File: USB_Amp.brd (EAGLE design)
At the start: 94 x 64 mm, 173 parts, among them CON1 USB-C-2OZ, CON2 PROG, CON3 PWR IN, CON5 SWD, CON6 USB-C-2OZ, IC1 3.3V, IC2 PIC32MZEF, IC3 TAS6422, IC4 3.3V, IC5 3.3V, IC6 TL431, IC7 STM32G030F, IC8 7805, IC9 CH221, Q1 NPN, Q2 NPN, Q3 PNP, Q4 PNP, X1 24.576MHz, X3 12MHz

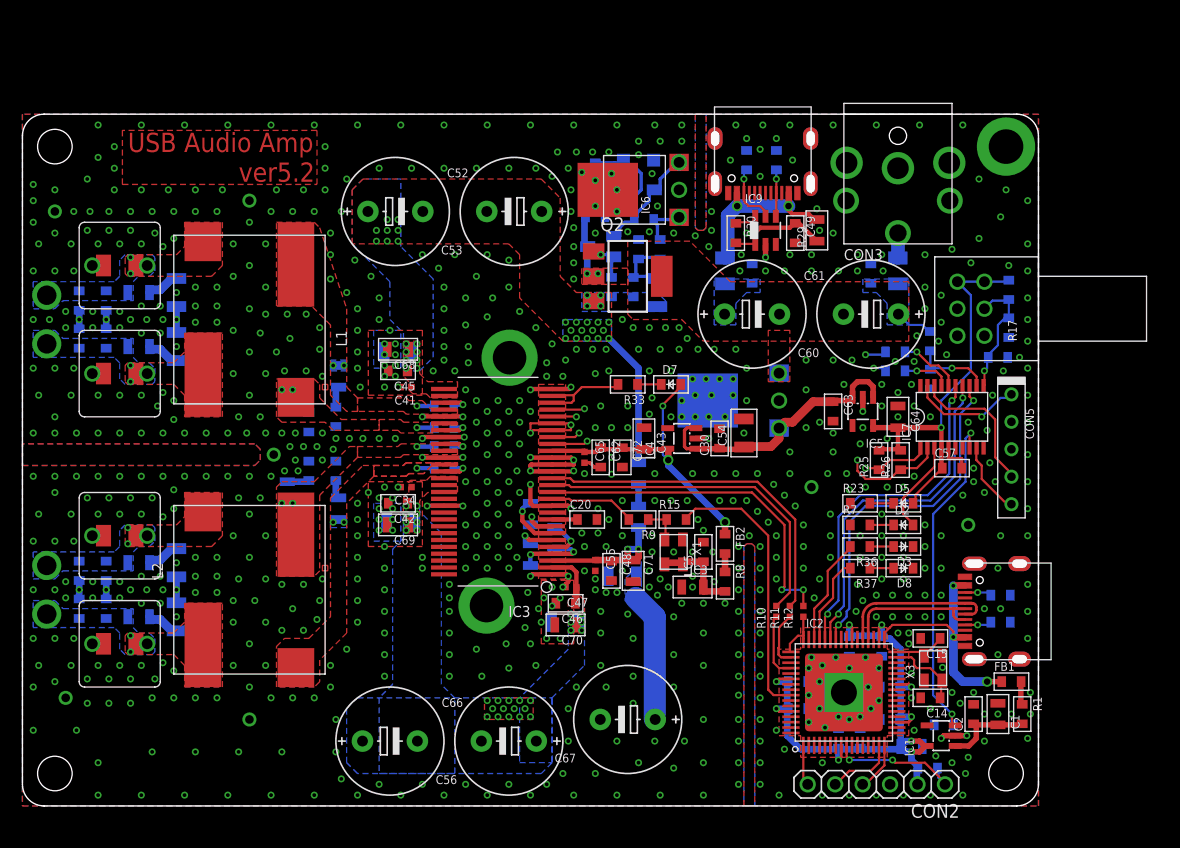
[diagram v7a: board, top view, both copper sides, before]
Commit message: TAS6424対応
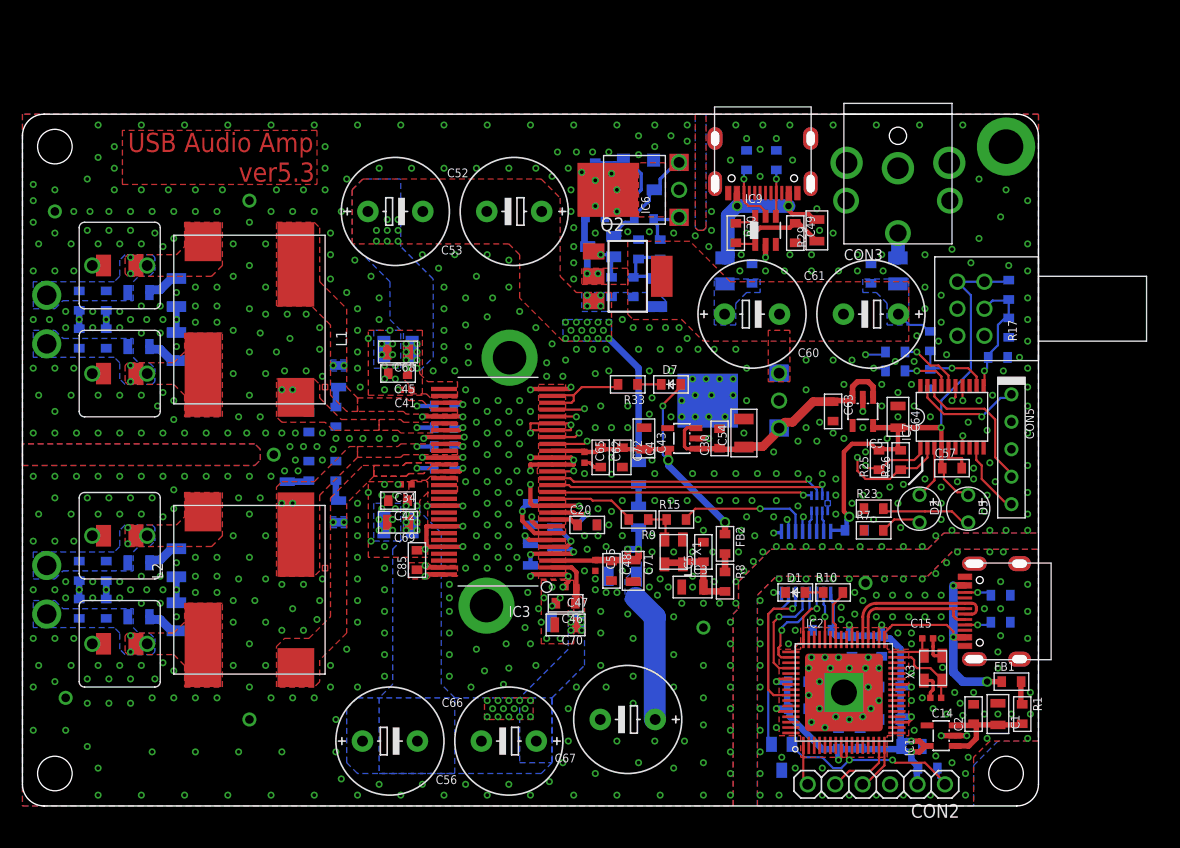
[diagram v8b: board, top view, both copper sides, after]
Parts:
- removed D3: LED1, my_rcl:D1608
- removed D8: LED2, my_rcl:D1608
- removed R11: DATA, my_rcl:1005
- removed R12: SCK, my_rcl:1005
- removed R36, R37: 3.3k, my_rcl:1608
- added C82, C83, C85: 0.1u, my_rcl:1608C
- added C84: 2.2u, my_rcl:1608C
- added D1: PLY, my_rcl:D1608
- added IC10: ISO7762, my_ic:TSSOP16
- added Q5: PNP, my_ic:SC59
- C14, C15: device my_rcl:1608C -> my_rcl:1005
- C74, C75: device my_rcl:3216 -> my_rcl:3225
- D2, D5: device my_rcl:D1608 -> my_rcl:LED2.5
- R10: value LRCLK -> 3.3k; device my_rcl:1005 -> my_rcl:1608
- R23, R7: value 3.3k -> 1.5k
- R6: value 10k -> 100; device my_rcl:1608 -> my_rcl:EXB28V
- moved TP10 26.3 mm to (63.0, 16.5)
- moved R6 23.5 mm to (73.8, 28.0)
- moved TP9 10.2 mm to (78.0, 20.6), turned to 0 degrees
- moved D5 6.02 mm to (87.5, 27.5), turned to 270 degrees
- moved R10 5.53 mm to (75.0, 19.8), turned to 0 degrees
- moved D2 2.12 mm to (83.0, 27.5), turned to 270 degrees
- moved R23 1.35 mm to (78.8, 27.5)
- moved R7 1.35 mm to (78.8, 25.5)
- moved C14 0.50 mm to (84.5, 10.0)
- moved C20 0.50 mm to (52.2, 26.0)
- moved C74 0.35 mm to (34.8, 26.0)
- moved C15 0.25 mm to (83.8, 15.5), turned to 0 degrees
- moved C34 0.25 mm to (35.5, 29.8)
- moved C41 0.25 mm to (35.5, 38.5)
- moved C42 0.25 mm to (34.8, 28.2)
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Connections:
- removed net EN_DDC: IC1.3, IC7.8, R6.1
- removed net LED2: IC2.45, R37.2
- removed net N$40: IC2.48, IC2.49, R12.1
- removed net N$41: IC2.50, R11.1
- removed net N$43: IC2.52, R10.1
- removed net N$44: D8.A, R37.1
- removed net PIC_COM2: IC2.43, IC7.14
- removed net PIC_COM3: IC2.42, IC7.13
- new net AMP_GVDD2: C84.1, IC3.10
- new net DGND: C1.2, C10.2, C11.2, C12.2, C13.2, C14.2, C15.2, C2.2, C4.2, C6.2, C7.2, C8.2, C82.2, C9.2, CON1.A1,B12:GND, CON1.B1,A12:GND, CON1.SHILED1, CON1.SHILED2, CON1.SHILED3, CON1.SHILED4, CON1.SHILED5, CON1.SHILED6, CON1.SHILED7, CON1.SHILED8, CON2.3, D1.K, IC1.2, IC10.8, IC2.20, IC2.25, IC2.35, IC2.40, IC2.55, IC2.59, IC2.7, IC2.HT, IC2.HT2, Q5.3, R2.1, R4.1, TP9.1, X3.2, X3.4
- new net I2S_MCLK2: IC10.11, R15.2
- new net N$10: IC10.15, R6.2
- new net N$11: IC10.14, R6.3
- new net N$12: IC10.13, R6.4
- new net PIC_DATA: IC10.4, IC2.50
- new net PIC_DDC_EN: IC10.7, Q5.1
- new net PIC_LRCLK: IC10.5, IC2.52
- new net PIC_SCK: IC10.3, IC2.48, IC2.49
- new net STM_COM1: IC10.12, IC7.14
- new net STM_DDC_EN: IC10.10, IC7.15
- net +3V3: now also C83.1, IC10.16
- net +3V3D: now also C82.1, IC10.1
- net GND: now also C83.2, C84.2, C85.2, IC10.9, IC3.49, IC3.52, R6.1, R6.8; no longer C1.2, C10.2, C11.2, C12.2, C13.2, C14.2, C15.2, C2.2, C4.2, C6.2, C7.2, C8.2, C9.2, CON1.A1,B12:GND, CON1.B1,A12:GND, CON1.SHILED1, CON1.SHILED2, CON1.SHILED3, CON1.SHILED4, CON1.SHILED5, CON1.SHILED6, CON1.SHILED7, CON1.SHILED8, CON2.3, D3.K, D8.K, IC1.2, IC2.20, IC2.25, IC2.35, IC2.40, IC2.55, IC2.59, IC2.7, IC2.HT, IC2.HT2, R2.1, R4.1, R6.2, TP9.1, X3.2, X3.4
- net I2S_DATA: now also R6.6; no longer R11.2
- net I2S_LRCLK: now also IC7.7, R6.7; no longer R10.2
- net I2S_SCK: now also R6.5; no longer R12.2
- net LED1: now also IC2.42, R10.2; no longer IC2.46, R36.2
- net MCLR: now also Q5.2
- net N$4: now also IC1.3
- net N$9: now also D1.A, R10.1; no longer D3.A, R36.1
- net PIC_COM1: now also IC10.2; no longer IC7.15
- net PIC_MCLK: now also IC10.6; no longer R15.2
- net PVDD: now also C85.1, IC3.55, IC3.56
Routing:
- net PIC_COM3: track 32.5 -> 0.00 mm, vias 2 -> 0
- net PIC_COM2: track 32.2 -> 0.00 mm, vias 2 -> 0
- net EN_DDC: track 31.8 -> 0.00 mm, vias 2 -> 0
- net STM_COM1: track 0.00 -> 29.4 mm, vias 0 -> 2
- net STM_DDC_EN: track 0.00 -> 28.5 mm, vias 0 -> 2
- net PIC_COM1: track 32.1 -> 4.25 mm, vias 2 -> 1
- net PIC_DDC_EN: track 0.00 -> 15.2 mm
- net I2S_MCLK2: track 0.00 -> 12.6 mm, vias 0 -> 1
- net +3V3: track 38.9 -> 51.4 mm, vias 1 -> 2
- net PIC_MCLK: track 25.7 -> 13.2 mm, vias 0 -> 1
- net I2S_LRCLK: track 31.7 -> 42.8 mm, vias 0 -> 2
- net PIC_LRCLK: track 0.00 -> 10.1 mm, vias 0 -> 1
- net PIC_DATA: track 0.00 -> 8.65 mm, vias 0 -> 1
- net I2S_SCK: track 32.4 -> 24.2 mm, vias 2 -> 1
- net LED2: track 8.13 -> 0.00 mm
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- added copper zone on layer 1, net DGND
- added copper zone on layer 15, net DGND
- added copper zone on layer 16, net DGND
- added copper zone on layer 2, net DGND
- added copper zone on layer 16, net GND]
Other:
- board text added: "ver5.3"
- board text removed: "10.9pF"
- board text removed: "15.2pF"
- board text removed: "17.9pF"
- board text removed: "19.3pF"
- board text removed: "ver5.2"
